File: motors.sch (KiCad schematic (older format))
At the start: 9 parts, among them M5 ALIS-CUSTOM-PARTS_POWERPADS, Q5 BSS138

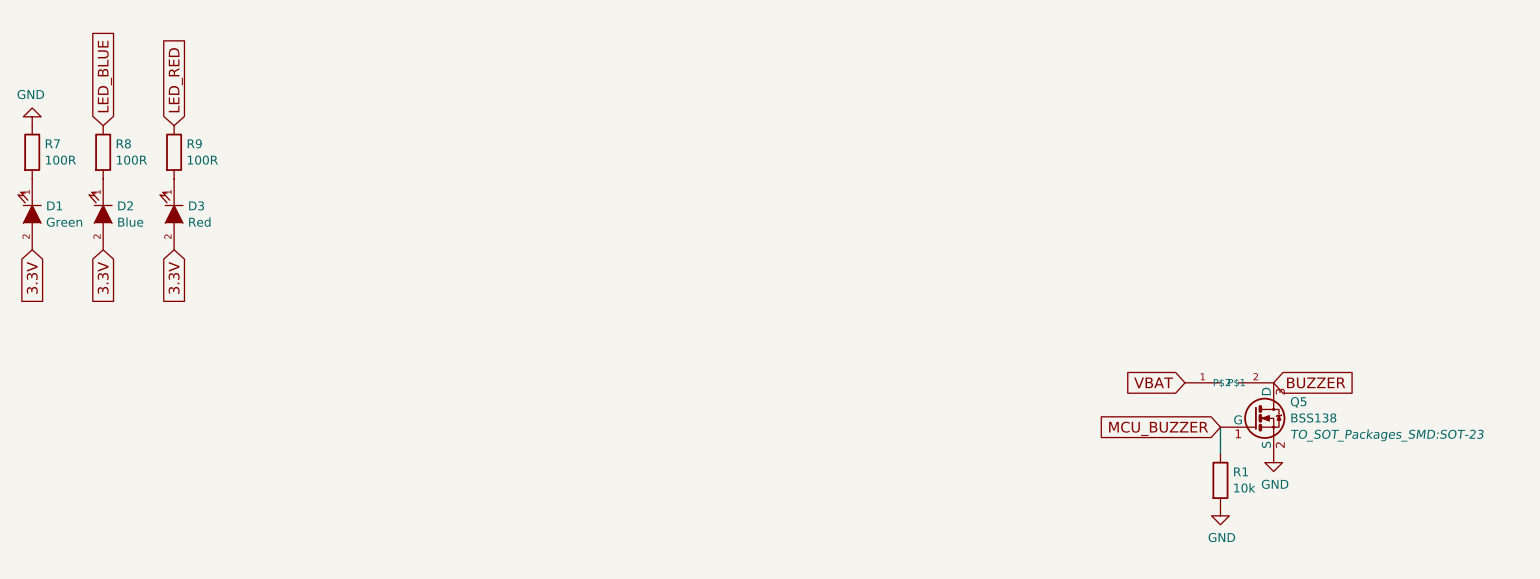
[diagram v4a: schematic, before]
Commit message: routing finished - essential signals only
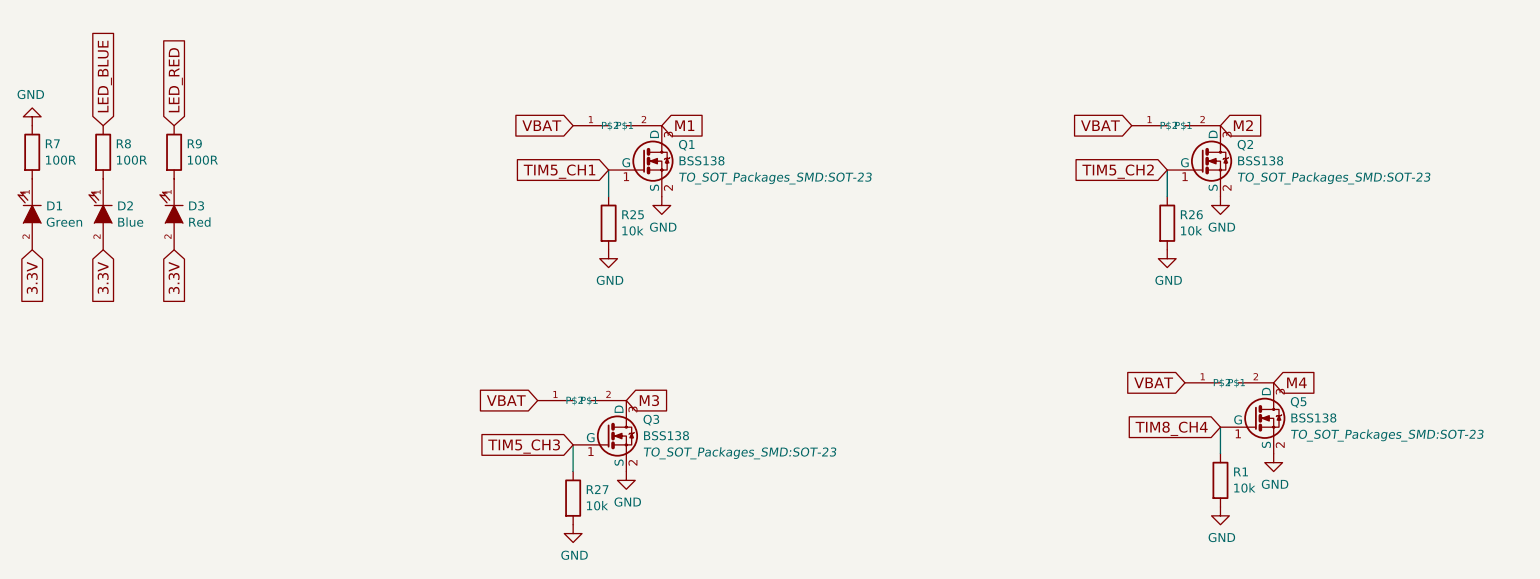
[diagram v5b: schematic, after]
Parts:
- added M1, M2, M3: ALIS-CUSTOM-PARTS_POWERPADS, alis_parts:motor_pads, symbol ALIS-CUSTOM-PARTS_POWERPADS
- added Q1, Q2, Q3: BSS138, TO_SOT_Packages_SMD:SOT-23, symbol BSS138
- added R25, R26, R27: 10k, Resistors_SMD:R_0402, symbol R
- D1, D2, D3: footprint LEDs:LED-0805 -> LEDs:LED-0603
- M5: footprint minimal:ALIS-CUSTOM-PARTS_PAD-JUMPER-2-NO_YES_SILK -> alis_parts:motor_pads
- R1, R7, R8, R9: footprint Resistors_SMD:R_0603 -> Resistors_SMD:R_0402
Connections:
- net GND: now also Q1.2 (S), Q2.2 (S), Q3.2 (S), R25.2, R26.2, R27.2
- net VBAT: now also M1.1 (P$1), M2.1 (P$1), M3.1 (P$1)
- net BUZZER renamed M4
- net MCU_BUZZER renamed TIM8_CH4
- new net M1: M1.2 (P$2), Q1.3 (D)
- new net M2: M2.2 (P$2), Q2.3 (D)
- new net M3: M3.2 (P$2), Q3.3 (D)
- new net TIM5_CH1: Q1.1 (G), R25.1
- new net TIM5_CH2: Q2.1 (G), R26.1
- new net TIM5_CH3: Q3.1 (G), R27.1
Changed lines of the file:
@@
 $Descr A4 11693 8268
 encoding utf-8
-Sheet 7 8
+Sheet 7 7
 Title ""
 Date ""
@@
 $EndDescr
 Text GLabel 8200 2950 2    60   Input ~ 0
-BUZZER
-$Comp
-L GND #PWR037
+M4
+$Comp
+L GND #PWR038
 U 1 1 569BDE16
 P 8200 3350
-F 0 "#PWR037" H 8200 3100 50  0001 C CNN
+F 0 "#PWR038" H 8200 3100 50  0001 C CNN
 F 1 "GND" H 8208 3176 50  0000 C CNN
 F 2 "" H 8200 3350 50  0000 C CNN
@@
 $EndComp
 Text GLabel 7900 3200 0    60   Input ~ 0
-MCU_BUZZER
+TIM8_CH4
 Text GLabel 7700 2950 0    60   Input ~ 0
 VBAT
@@
 F 0 "M5" H 8000 2950 50  0001 C CNN
 F 1 "ALIS-CUSTOM-PARTS_POWERPADS" H 8000 2950 50  0001 C CNN
-F 2 "minimal:ALIS-CUSTOM-PARTS_PAD-JUMPER-2-NO_YES_SILK" H 8030 3100 20  0001 C CNN
+F 2 "alis_parts:motor_pads" H 8030 3100 20  0001 C CNN
 F 3 "" H 8000 2950 60  0000 C CNN
 	1    8000 2950
@@
 F 0 "D3" V 1954 2078 50  0000 L CNN
 F 1 "Red" V 2046 2078 50  0000 L CNN
-F 2 "LEDs:LED-0805" H 2000 2000 50  0001 C CNN
+F 2 "LEDs:LED-0603" H 2000 2000 50  0001 C CNN
 F 3 "" H 2000 2000 50  0000 C CNN
 	1    2000 2000
@@
 F 0 "D2" V 1554 2078 50  0000 L CNN
 F 1 "Blue" V 1646 2078 50  0000 L CNN
-F 2 "LEDs:LED-0805" H 1600 2000 50  0001 C CNN
+F 2 "LEDs:LED-0603" H 1600 2000 50  0001 C CNN
 F 3 "" H 1600 2000 50  0000 C CNN
 	1    1600 2000
@@
 F 0 "D1" V 1154 2078 50  0000 L CNN
 F 1 "Green" V 1246 2078 50  0000 L CNN
-F 2 "LEDs:LED-0805" H 1200 2000 50  0001 C CNN
+F 2 "LEDs:LED-0603" H 1200 2000 50  0001 C CNN
 F 3 "" H 1200 2000 50  0000 C CNN
 	1    1200 2000
@@
 3.3V
 $Comp
-L GND #PWR038
+L GND #PWR039
 U 1 1 569BFFAD
 P 1200 1500
-F 0 "#PWR038" H 1200 1250 50  0001 C CNN
+F 0 "#PWR039" H 1200 1250 50  0001 C CNN
 F 1 "GND" H 1208 1326 50  0000 C CNN
 F 2 "" H 1200 1500 50  0000 C CNN
@@
 F 0 "R9" H 2070 1696 50  0000 L CNN
 F 1 "100R" H 2070 1604 50  0000 L CNN
-F 2 "Resistors_SMD:R_0603" V 1930 1650 50  0001 C CNN
+F 2 "Resistors_SMD:R_0402" V 1930 1650 50  0001 C CNN
 F 3 "" H 2000 1650 50  0000 C CNN
 	1    2000 1650
@@
 F 0 "R8" H 1670 1696 50  0000 L CNN
 F 1 "100R" H 1670 1604 50  0000 L CNN
-F 2 "Resistors_SMD:R_0603" V 1530 1650 50  0001 C CNN
+F 2 "Resistors_SMD:R_0402" V 1530 1650 50  0001 C CNN
 F 3 "" H 1600 1650 50  0000 C CNN
 	1    1600 1650
@@
 F 0 "R7" H 1270 1696 50  0000 L CNN
 F 1 "100R" H 1270 1604 50  0000 L CNN
-F 2 "Resistors_SMD:R_0603" V 1130 1650 50  0001 C CNN
+F 2 "Resistors_SMD:R_0402" V 1130 1650 50  0001 C CNN
 F 3 "" H 1200 1650 50  0000 C CNN
 	1    1200 1650
@@
 F 0 "R1" H 7970 3546 50  0000 L CNN
 F 1 "10k" H 7970 3455 50  0000 L CNN
-F 2 "Resistors_SMD:R_0603" V 7830 3500 50  0001 C CNN
+F 2 "Resistors_SMD:R_0402" V 7830 3500 50  0001 C CNN
 F 3 "" H 7900 3500 50  0000 C CNN
 	1    7900 3500
@@
 $EndComp
 $Comp
-L GND #PWR039
+L GND #PWR040
 U 1 1 57268FA8
 P 7900 3650
-F 0 "#PWR039" H 7900 3400 50  0001 C CNN
+F 0 "#PWR040" H 7900 3400 50  0001 C CNN
 F 1 "GND" H 7908 3476 50  0000 C CNN
 F 2 "" H 7900 3650 50  0000 C CNN
@@
 Wire Wire Line
 	7900 3350 7900 3200
+Text GLabel 4750 1500 2    60   Input ~ 0
+M1
+$Comp
+L GND #PWR041
+U 1 1 575DB24D
+P 4750 1900
+F 0 "#PWR041" H 4750 1650 50  0001 C CNN
+F 1 "GND" H 4758 1726 50  0000 C CNN
+F 2 "" H 4750 1900 50  0000 C CNN
+F 3 "" H 4750 1900 50  0000 C CNN
+	1    4750 1900
+	1    0    0    -1
+$EndComp
+Text GLabel 4450 1750 0    60   Input ~ 0
+TIM5_CH1
+Text GLabel 4250 1500 0    60   Input ~ 0
+VBAT
+$Comp
+L ALIS-CUSTOM-PARTS_POWERPADS M?
+U 1 1 575DB255
+P 4550 1500
+AR Path="/575DB255" Ref="M?"  Part="1"
+AR Path="/56980F2E/575DB255" Ref="M1"  Part="1"
+F 0 "M1" H 4550 1500 50  0001 C CNN
+F 1 "ALIS-CUSTOM-PARTS_POWERPADS" H 4550 1500 50  0001 C CNN
+F 2 "alis_parts:motor_pads" H 4580 1650 20  0001 C CNN
+F 3 "" H 4550 1500 60  0000 C CNN
+	1    4550 1500
+	0    -1   -1   0
+$EndComp
+$Comp
+L BSS138 Q1
+U 1 1 575DB25B
+P 4650 1700
+F 0 "Q1" H 4843 1792 50  0000 L CNN
+F 1 "BSS138" H 4843 1700 50  0000 L CNN
+F 2 "TO_SOT_Packages_SMD:SOT-23" H 4843 1608 50  0000 L CIN
+F 3 "" H 4650 1700 50  0000 L CNN
+	1    4650 1700
+	1    0    0    -1
+$EndComp
+$Comp
+L R R25
+U 1 1 575DB262
+P 4450 2050
+F 0 "R25" H 4520 2096 50  0000 L CNN
+F 1 "10k" H 4520 2005 50  0000 L CNN
+F 2 "Resistors_SMD:R_0402" V 4380 2050 50  0001 C CNN
+F 3 "" H 4450 2050 50  0000 C CNN
+	1    4450 2050
+	1    0    0    -1
+$EndComp
+$Comp
+L GND #PWR042
+U 1 1 575DB269
+P 4450 2200
+F 0 "#PWR042" H 4450 1950 50  0001 C CNN
+F 1 "GND" H 4458 2026 50  0000 C CNN
+F 2 "" H 4450 2200 50  0000 C CNN
+F 3 "" H 4450 2200 50  0000 C CNN
+	1    4450 2200
+	1    0    0    -1
+$EndComp
+Wire Wire Line
+	4450 1900 4450 1750
+Text GLabel 4550 3050 2    60   Input ~ 0
+M3
+$Comp
+L GND #PWR043
+U 1 1 575DB303
+P 4550 3450
+F 0 "#PWR043" H 4550 3200 50  0001 C CNN
+F 1 "GND" H 4558 3276 50  0000 C CNN
+F 2 "" H 4550 3450 50  0000 C CNN
+F 3 "" H 4550 3450 50  0000 C CNN
+	1    4550 3450
+	1    0    0    -1
+$EndComp
+Text GLabel 4250 3300 0    60   Input ~ 0
+TIM5_CH3
+Text GLabel 4050 3050 0    60   Input ~ 0
+VBAT
+$Comp
+L ALIS-CUSTOM-PARTS_POWERPADS M?
+U 1 1 575DB30B
+P 4350 3050
+AR Path="/575DB30B" Ref="M?"  Part="1"
+AR Path="/56980F2E/575DB30B" Ref="M3"  Part="1"
+F 0 "M3" H 4350 3050 50  0001 C CNN
+F 1 "ALIS-CUSTOM-PARTS_POWERPADS" H 4350 3050 50  0001 C CNN
+F 2 "alis_parts:motor_pads" H 4380 3200 20  0001 C CNN
+F 3 "" H 4350 3050 60  0000 C CNN
+	1    4350 3050
+	0    -1   -1   0
+$EndComp
+$Comp
+L BSS138 Q3
+U 1 1 575DB311
+P 4450 3250
+F 0 "Q3" H 4643 3342 50  0000 L CNN
+F 1 "BSS138" H 4643 3250 50  0000 L CNN
+F 2 "TO_SOT_Packages_SMD:SOT-23" H 4643 3158 50  0000 L CIN
+F 3 "" H 4450 3250 50  0000 L CNN
+	1    4450 3250
+	1    0    0    -1
+$EndComp
+$Comp
+L R R27
+U 1 1 575DB318
+P 4250 3600
+F 0 "R27" H 4320 3646 50  0000 L CNN
+F 1 "10k" H 4320 3555 50  0000 L CNN
+F 2 "Resistors_SMD:R_0402" V 4180 3600 50  0001 C CNN
+F 3 "" H 4250 3600 50  0000 C CNN
+	1    4250 3600
+	1    0    0    -1
+$EndComp
+$Comp
+L GND #PWR044
+U 1 1 575DB31F
+P 4250 3750
+F 0 "#PWR044" H 4250 3500 50  0001 C CNN
+F 1 "GND" H 4258 3576 50  0000 C CNN
+F 2 "" H 4250 3750 50  0000 C CNN
+F 3 "" H 4250 3750 50  0000 C CNN
+	1    4250 3750
+	1    0    0    -1
+$EndComp
+Wire Wire Line
+	4250 3450 4250 3300
+Text GLabel 7900 1500 2    60   Input ~ 0
+M2
+$Comp
+L GND #PWR045
+U 1 1 575DB3A7
+P 7900 1900
+F 0 "#PWR045" H 7900 1650 50  0001 C CNN
+F 1 "GND" H 7908 1726 50  0000 C CNN
+F 2 "" H 7900 1900 50  0000 C CNN
+F 3 "" H 7900 1900 50  0000 C CNN
+	1    7900 1900
+	1    0    0    -1
+$EndComp
+Text GLabel 7600 1750 0    60   Input ~ 0
+TIM5_CH2
+Text GLabel 7400 1500 0    60   Input ~ 0
+VBAT
+$Comp
+L ALIS-CUSTOM-PARTS_POWERPADS M?
+U 1 1 575DB3AF
+P 7700 1500
+AR Path="/575DB3AF" Ref="M?"  Part="1"
+AR Path="/56980F2E/575DB3AF" Ref="M2"  Part="1"
+F 0 "M2" H 7700 1500 50  0001 C CNN
+F 1 "ALIS-CUSTOM-PARTS_POWERPADS" H 7700 1500 50  0001 C CNN
+F 2 "alis_parts:motor_pads" H 7730 1650 20  0001 C CNN
+F 3 "" H 7700 1500 60  0000 C CNN
+	1    7700 1500
+	0    -1   -1   0
+$EndComp
+$Comp
+L BSS138 Q2
+U 1 1 575DB3B5
+P 7800 1700
+F 0 "Q2" H 7993 1792 50  0000 L CNN
+F 1 "BSS138" H 7993 1700 50  0000 L CNN
+F 2 "TO_SOT_Packages_SMD:SOT-23" H 7993 1608 50  0000 L CIN
+F 3 "" H 7800 1700 50  0000 L CNN
+	1    7800 1700
+	1    0    0    -1
+$EndComp
+$Comp
+L R R26
+U 1 1 575DB3BC
+P 7600 2050
+F 0 "R26" H 7670 2096 50  0000 L CNN
+F 1 "10k" H 7670 2005 50  0000 L CNN
+F 2 "Resistors_SMD:R_0402" V 7530 2050 50  0001 C CNN
+F 3 "" H 7600 2050 50  0000 C CNN
+	1    7600 2050
+	1    0    0    -1
+$EndComp
+$Comp
+L GND #PWR046
+U 1 1 575DB3C3
+P 7600 2200
+F 0 "#PWR046" H 7600 1950 50  0001 C CNN
+F 1 "GND" H 7608 2026 50  0000 C CNN
+F 2 "" H 7600 2200 50  0000 C CNN
+F 3 "" H 7600 2200 50  0000 C CNN
+	1    7600 2200
+	1    0    0    -1
+$EndComp
+Wire Wire Line
+	7600 1900 7600 1750
 $EndSCHEMATC

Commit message: minor changes
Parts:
- removed D3: Red, LEDs:LED-0603, symbol LED
- removed R9: 100R, Resistors_SMD:R_0402, symbol R
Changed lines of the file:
@@
 M4
 $Comp
-L GND #PWR038
+L GND #PWR039
 U 1 1 569BDE16
 P 8200 3350
-F 0 "#PWR038" H 8200 3100 50  0001 C CNN
+F 0 "#PWR039" H 8200 3100 50  0001 C CNN
 F 1 "GND" H 8208 3176 50  0000 C CNN
 F 2 "" H 8200 3350 50  0000 C CNN
@@
 $EndComp
 $Comp
-L LED D3
-U 1 1 569BFF96
-P 2000 2000
-F 0 "D3" V 1954 2078 50  0000 L CNN
-F 1 "Red" V 2046 2078 50  0000 L CNN
-F 2 "LEDs:LED-0603" H 2000 2000 50  0001 C CNN
-F 3 "" H 2000 2000 50  0000 C CNN
-	1    2000 2000
-	0    1    1    0
-$EndComp
-$Comp
 L LED D2
 U 1 1 569BFF9D
@@
 	0    1    1    0
 $EndComp
-Text GLabel 2000 2200 3    60   Input ~ 0
-3.3V
 Text GLabel 1600 2200 3    60   Input ~ 0
 3.3V
 $Comp
-L GND #PWR039
+L GND #PWR040
 U 1 1 569BFFAD
 P 1200 1500
-F 0 "#PWR039" H 1200 1250 50  0001 C CNN
+F 0 "#PWR040" H 1200 1250 50  0001 C CNN
 F 1 "GND" H 1208 1326 50  0000 C CNN
 F 2 "" H 1200 1500 50  0000 C CNN
@@
 Text GLabel 1200 2200 3    60   Input ~ 0
 3.3V
-Text GLabel 2000 1500 1    60   Input ~ 0
-LED_RED
 Text GLabel 1600 1500 1    60   Input ~ 0
 LED_BLUE
-$Comp
-L R R9
-U 1 1 569BFFB6
-P 2000 1650
-F 0 "R9" H 2070 1696 50  0000 L CNN
-F 1 "100R" H 2070 1604 50  0000 L CNN
-F 2 "Resistors_SMD:R_0402" V 1930 1650 50  0001 C CNN
-F 3 "" H 2000 1650 50  0000 C CNN
-	1    2000 1650
-	1    0    0    -1
-$EndComp
 $Comp
 L R R8
@@
 $EndComp
 $Comp
-L GND #PWR040
+L GND #PWR041
 U 1 1 57268FA8
 P 7900 3650
-F 0 "#PWR040" H 7900 3400 50  0001 C CNN
+F 0 "#PWR041" H 7900 3400 50  0001 C CNN
 F 1 "GND" H 7908 3476 50  0000 C CNN
 F 2 "" H 7900 3650 50  0000 C CNN
@@
 M1
 $Comp
-L GND #PWR041
+L GND #PWR042
 U 1 1 575DB24D
 P 4750 1900
-F 0 "#PWR041" H 4750 1650 50  0001 C CNN
+F 0 "#PWR042" H 4750 1650 50  0001 C CNN
 F 1 "GND" H 4758 1726 50  0000 C CNN
 F 2 "" H 4750 1900 50  0000 C CNN
@@
 $EndComp
 $Comp
-L GND #PWR042
+L GND #PWR043
 U 1 1 575DB269
 P 4450 2200
-F 0 "#PWR042" H 4450 1950 50  0001 C CNN
+F 0 "#PWR043" H 4450 1950 50  0001 C CNN
 F 1 "GND" H 4458 2026 50  0000 C CNN
 F 2 "" H 4450 2200 50  0000 C CNN
@@
 M3
 $Comp
-L GND #PWR043
+L GND #PWR044
 U 1 1 575DB303
 P 4550 3450
-F 0 "#PWR043" H 4550 3200 50  0001 C CNN
+F 0 "#PWR044" H 4550 3200 50  0001 C CNN
 F 1 "GND" H 4558 3276 50  0000 C CNN
 F 2 "" H 4550 3450 50  0000 C CNN
@@
 $EndComp
 $Comp
-L GND #PWR044
+L GND #PWR045
 U 1 1 575DB31F
 P 4250 3750
-F 0 "#PWR044" H 4250 3500 50  0001 C CNN
+F 0 "#PWR045" H 4250 3500 50  0001 C CNN
 F 1 "GND" H 4258 3576 50  0000 C CNN
 F 2 "" H 4250 3750 50  0000 C CNN
@@
 M2
 $Comp
-L GND #PWR045
+L GND #PWR046
 U 1 1 575DB3A7
 P 7900 1900
-F 0 "#PWR045" H 7900 1650 50  0001 C CNN
+F 0 "#PWR046" H 7900 1650 50  0001 C CNN
 F 1 "GND" H 7908 1726 50  0000 C CNN
 F 2 "" H 7900 1900 50  0000 C CNN
@@
 $EndComp
 $Comp
-L GND #PWR046
+L GND #PWR047
 U 1 1 575DB3C3
 P 7600 2200
-F 0 "#PWR046" H 7600 1950 50  0001 C CNN
+F 0 "#PWR047" H 7600 1950 50  0001 C CNN
 F 1 "GND" H 7608 2026 50  0000 C CNN
 F 2 "" H 7600 2200 50  0000 C CNN

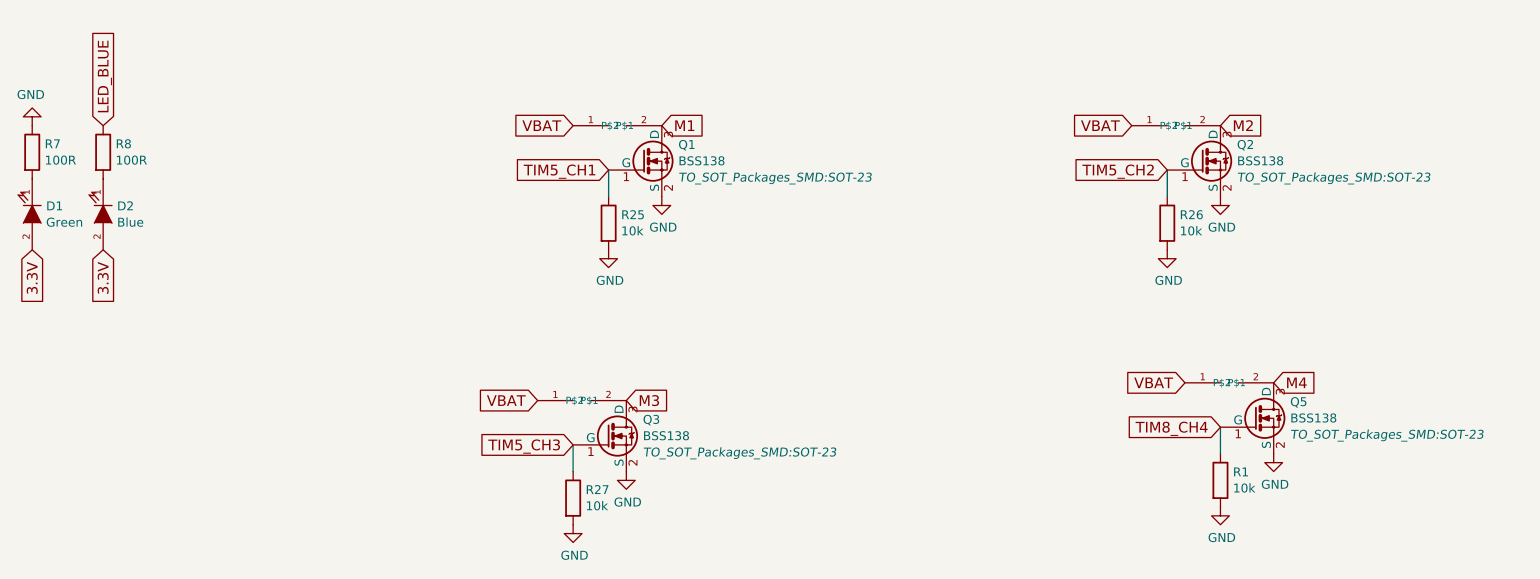
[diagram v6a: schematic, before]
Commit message: fixing switch polarity
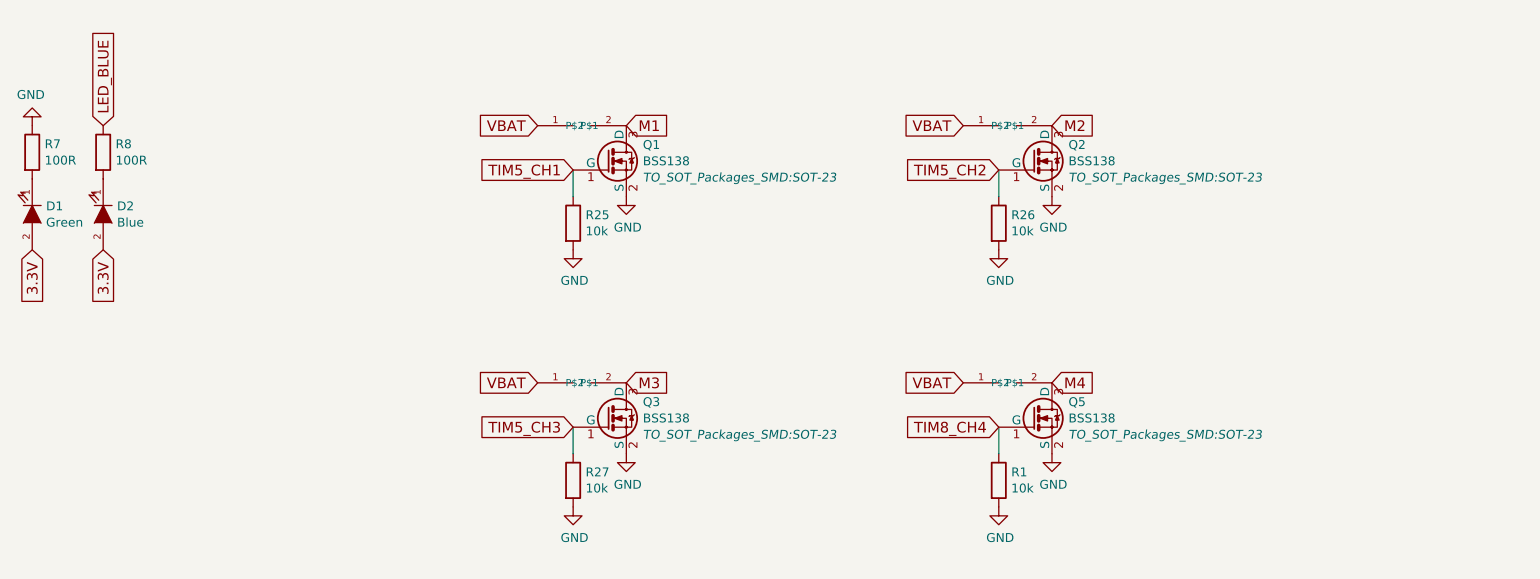
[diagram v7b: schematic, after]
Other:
- moved on the sheet: Q1, Q2, Q3, Q5, R1, R25, R26, R27
